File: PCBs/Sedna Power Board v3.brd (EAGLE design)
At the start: 50 x 32 mm, 21 parts

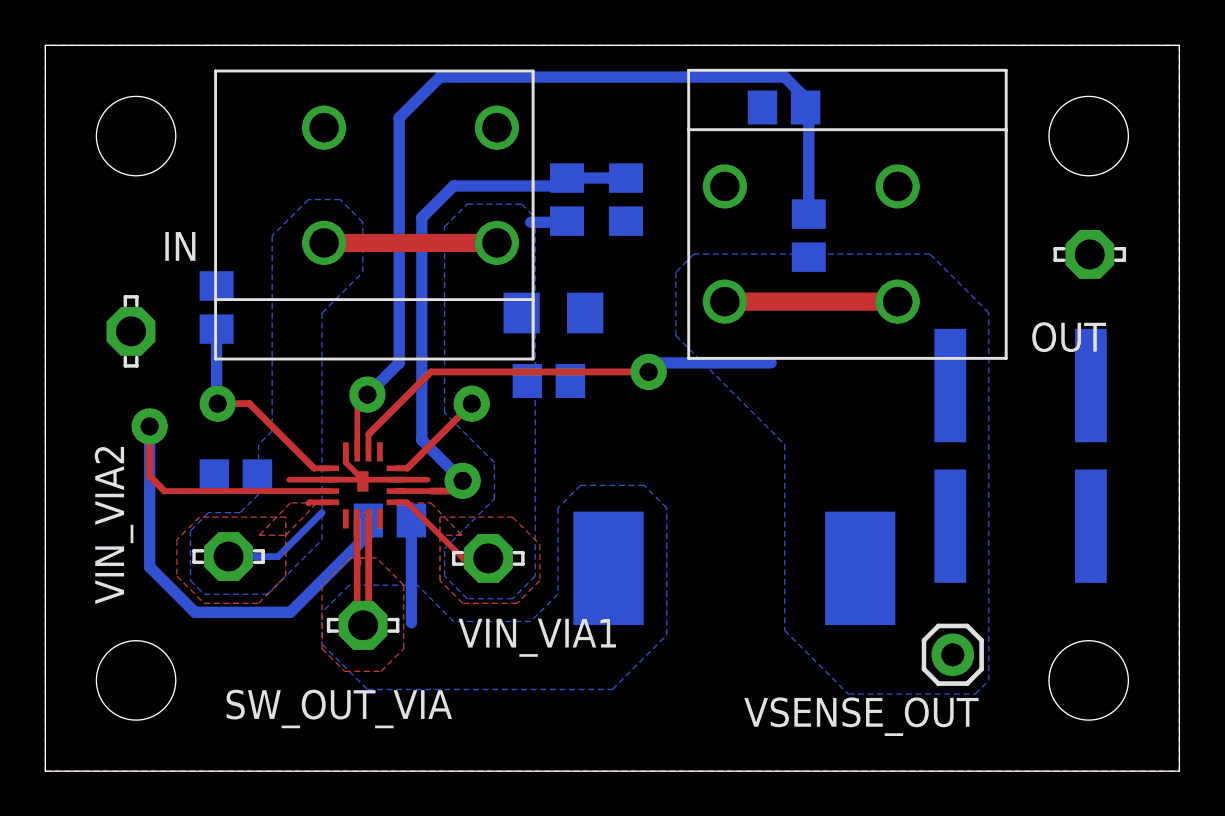
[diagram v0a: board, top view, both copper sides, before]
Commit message: v3 of the power board, now with a trimpot on the FB voltage divider for output voltage adjustments.
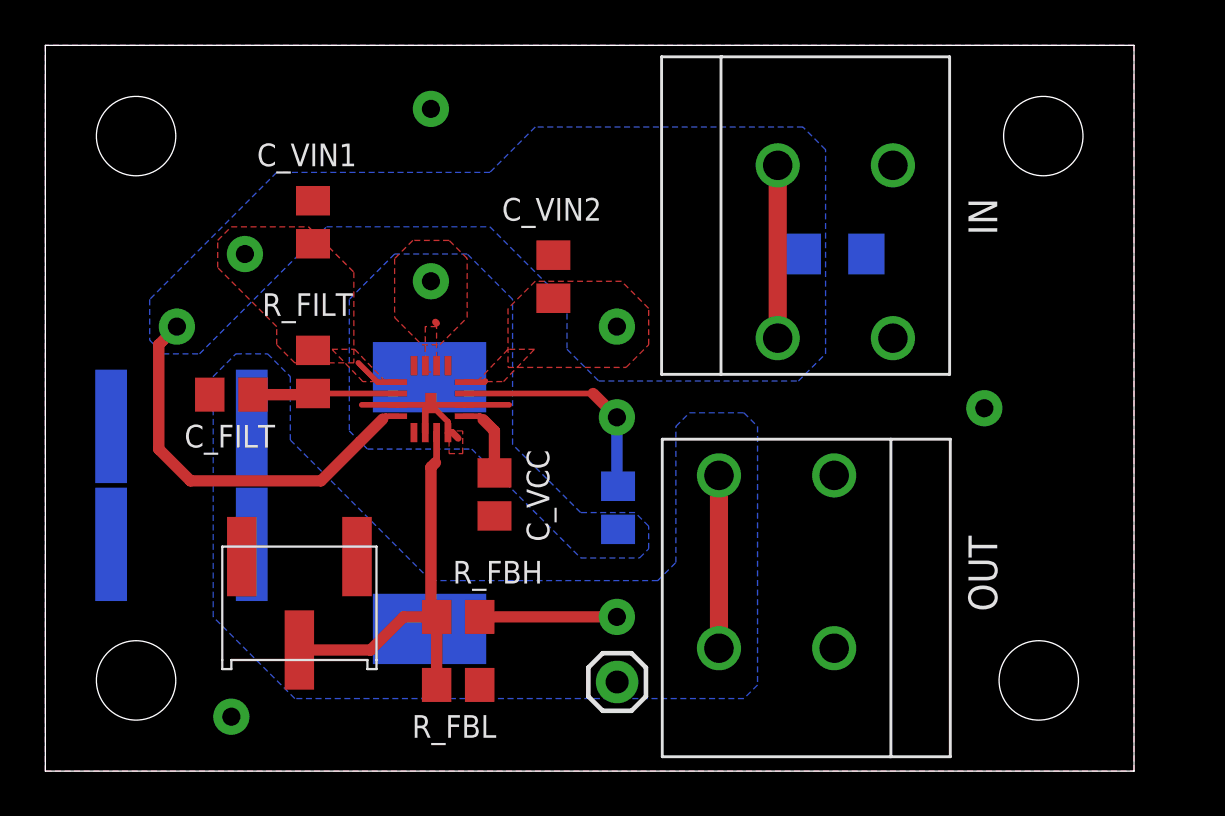
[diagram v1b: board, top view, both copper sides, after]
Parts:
- removed GND_VIA1, GND_VIA2, SW_OUT_VIA, VIN_VIA1, VIN_VIA2: LSP13, solpad:LSP13
- added TRIMMER: (no value), Sedna Components:BOURNS_3361S
- moved C_OUT_2 37.0 mm to (6.00, 15.2), turned to 0 degrees
- moved C_OUT_1 37.0 mm to (6.00, 10.0), turned to 0 degrees
- moved R_FBL 29.2 mm to (18.2, 3.80), flipped to the top
- moved R_FBH 22.8 mm to (18.2, 6.80), flipped to the top, turned to 180 degrees
- moved C_FILT 19.4 mm to (8.20, 16.6), flipped to the top, turned to 180 degrees
- moved IN 19.0 mm to (34.8, 22.9), turned to 180 degrees
- moved C_VIN2 16.5 mm to (22.4, 21.8), flipped to the top, turned to 90 degrees
- moved VSENSE_OUT 14.8 mm to (25.2, 3.93)
- moved C_VCC 14.8 mm to (19.8, 12.2), flipped to the top, turned to 270 degrees
- moved OUT 14.1 mm to (32.2, 9.23), turned to 0 degrees
- moved L_OUT 13.7 mm to (16.9, 11.8), turned to 0 degrees
- moved R_FILT 13.5 mm to (11.8, 17.6), flipped to the top, turned to 90 degrees
- moved C_IN 12.7 mm to (34.8, 22.8)
- moved C_VIN1 12.5 mm to (11.8, 24.2), flipped to the top, turned to 90 degrees
- moved C_BOOT 10.1 mm to (25.2, 11.6), turned to 270 degrees
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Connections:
- net FB: now also TRIMMER.2
- net GND: now also REGULATOR.6_VBIAS, TRIMMER.1; no longer GND_VIA1.MP, GND_VIA2.MP
- net SW_OUT: no longer SW_OUT_VIA.MP
- net V_IN: no longer VIN_VIA1.MP, VIN_VIA2.MP
- net V_OUT: no longer REGULATOR.6_VBIAS
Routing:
- net FB: track 40.2 -> 18.0 mm, vias 1 -> 0
- net C_BOOT: track 29.1 -> 10.2 mm
- net VINLDO: track 25.2 -> 6.40 mm, vias 1 -> 0
- net SW_OUT: track 14.2 -> 0.07 mm, vias 0 -> 1
- net V_OUT: track 27.4 -> 13.7 mm
- net VCC: track 9.42 -> 3.49 mm, vias 1 -> 0
- net V_IN: track 24.8 -> 28.7 mm, vias 1 -> 3
- net GND: track 7.75 -> 10.1 mm, vias 0 -> 3
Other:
- board size 50 x 32 mm -> 48 x 32 mm
- board text added: "Sedna Power Board v3.0"
- board text removed: "Sedna Power Board v2.0.2"
